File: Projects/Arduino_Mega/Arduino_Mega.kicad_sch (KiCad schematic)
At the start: 7 parts, among them J1 Power, J2 PWM, J3 Analog, J4 PWM, J5 Analog, J6 Communication, J7 Digital

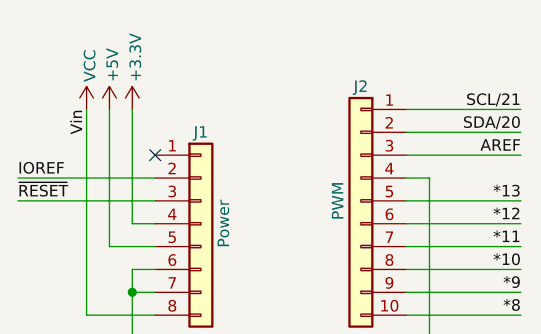
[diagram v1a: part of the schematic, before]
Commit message: Update templates to V8 format
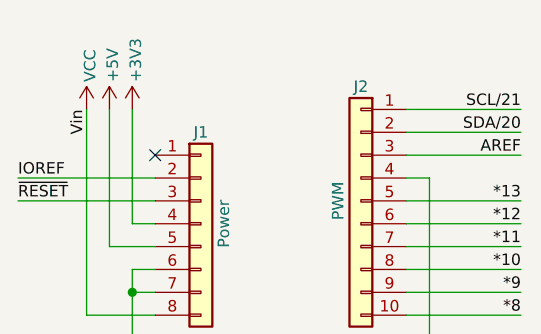
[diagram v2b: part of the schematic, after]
